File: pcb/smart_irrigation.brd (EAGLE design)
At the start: 100 x 80 mm, 17 parts, among them IC1 7805DT, IC2 7833DT, J1 1X2-3.5MM

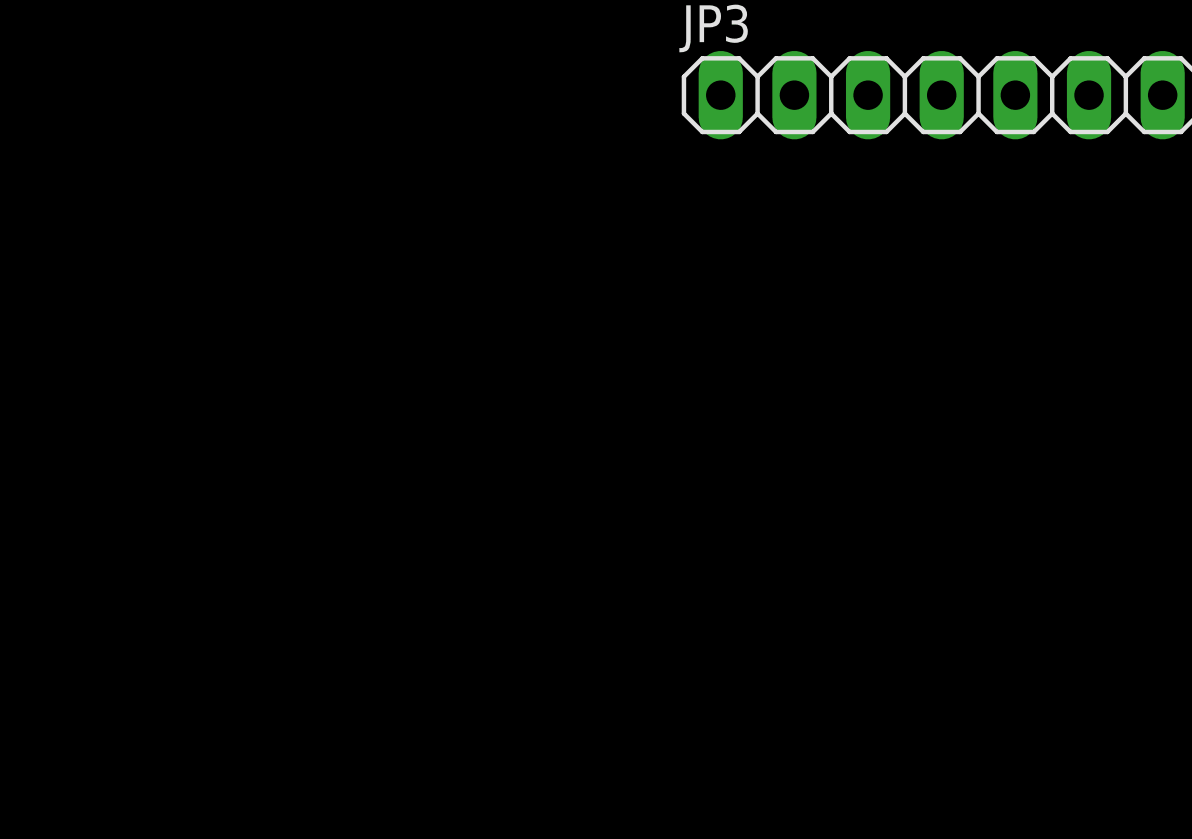
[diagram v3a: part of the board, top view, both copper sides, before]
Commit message: PCB: Add RTC
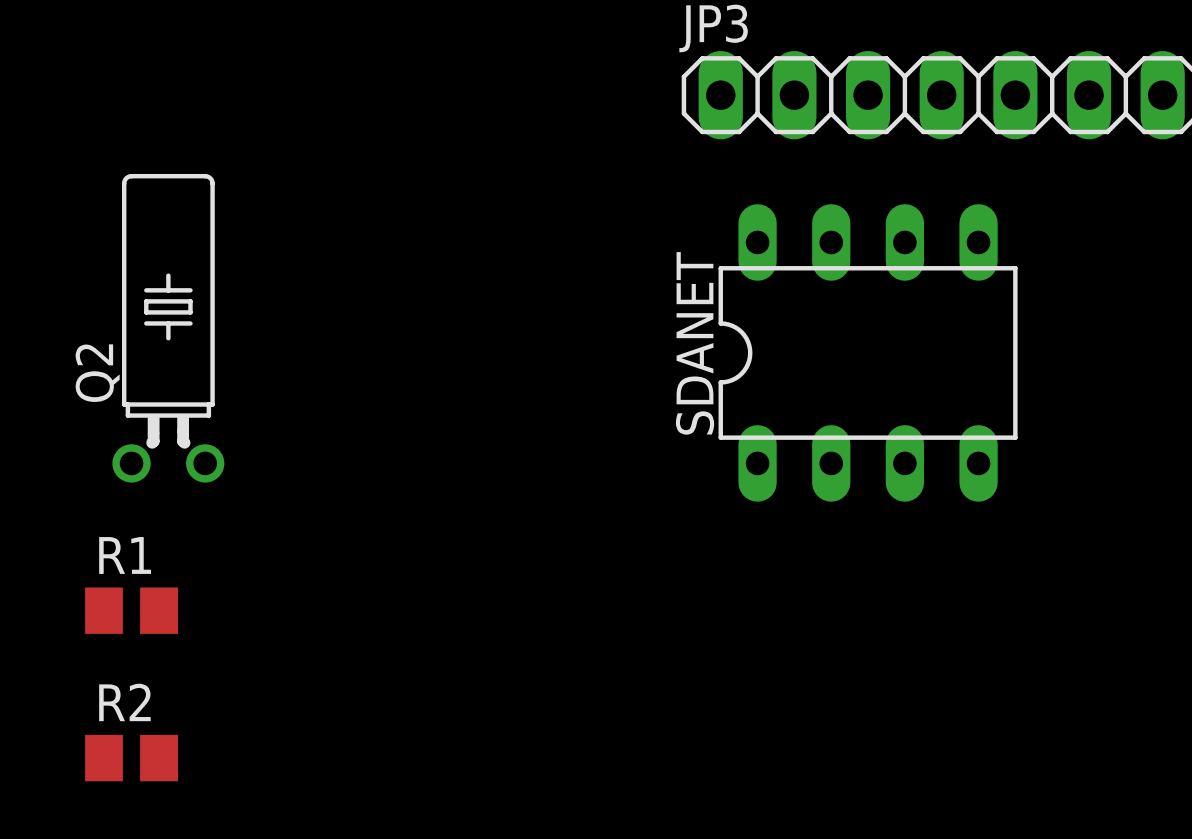
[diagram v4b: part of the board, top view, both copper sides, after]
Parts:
- added Q2: 32.768, crystal:TC38H
- added R1, R2: 2.2k, rcl:M0805
- added SDANET: DS1307, adafruit:DIL08
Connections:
- removed net N$17: JP3.3, U$1.26
- removed net N$28: JP3.14, U$1.13
- removed net N$29: JP3.15, U$1.12
- new net N$15: Q2.2, SDANET.2
- new net N$3: Q2.1, SDANET.1
- new net RTC_OUT: JP3.3, SDANET.7, U$1.26
- new net SCL: JP3.14, R2.1, SDANET.6, U$1.13
- new net SDA: JP3.15, R1.1, SDANET.5, U$1.12
- new net VBAT: SDANET.3
- net +3V3: now also R1.2, R2.2
- net +5V: now also SDANET.8
- net GND: now also SDANET.4
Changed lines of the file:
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@@
 <element name="JP2" library="pinhead" package="1X12" value="" x="-39.37" y="-101.6"/>
 <element name="JP3" library="pinhead" package="1X16" value="" x="-34.29" y="-107.95"/>
+<element name="SDANET" library="adafruit" package="DIL08" value="DS1307" x="-48.26" y="-116.84"/>
+<element name="Q2" library="crystal" package="TC38H" value="32.768" x="-72.39" y="-120.65">
+<attribute name="MPN" value="" x="-72.39" y="-120.65" size="1.778" layer="27" display="off"/>
+<attribute name="OC_NEWARK" value="unknown" x="-72.39" y="-120.65" size="1.778" layer="27" display="off"/>
+<attribute name="OC_FARNELL" value="unknown" x="-72.39" y="-120.65" size="1.778" layer="27" display="off"/>
+<attribute name="MF" value="" x="-72.39" y="-120.65" size="1.778" layer="27" display="off"/>
+</element>
+<element name="R1" library="rcl" package="M0805" value="2.2k" x="-73.66" y="-125.73"/>
+<element name="R2" library="rcl" package="M0805" value="2.2k" x="-73.66" y="-130.81"/>
 </elements>
 <signals>
@@
 <contactref element="U$1" pad="29"/>
 <contactref element="JP2" pad="1"/>
+<contactref element="SDANET" pad="4"/>
+<wire x1="-53.34" y1="-107.95" x2="-44.45" y2="-120.65" width="0" layer="19" extent="1-1"/>
 <wire x1="-53.34" y1="-101.6" x2="-53.34" y2="-107.95" width="0" layer="19" extent="1-1"/>
 <wire x1="-52.07" y1="-95.25" x2="-53.34" y2="-101.6" width="0" layer="19" extent="1-1"/>
@@
 <contactref element="C1" pad="1"/>
 <contactref element="C7" pad="1"/>
+<contactref element="SDANET" pad="8"/>
+<wire x1="-30.16" y1="-63.5" x2="-52.07" y2="-113.03" width="0" layer="19" extent="1-1"/>
 <wire x1="-30.16" y1="-25.4" x2="-30.16" y2="-63.5" width="0" layer="19" extent="1-1"/>
 <wire x1="-4.07" y1="1.55" x2="-30.16" y2="-25.4" width="0" layer="19" extent="1-1"/>
@@
 <contactref element="U$1" pad="J5_3"/>
 <contactref element="U$1" pad="J5_6"/>
+<contactref element="R2" pad="2"/>
+<contactref element="R1" pad="2"/>
+<wire x1="-72.71" y1="-125.73" x2="-72.71" y2="-130.81" width="0" layer="19" extent="1-1"/>
+<wire x1="-46.99" y1="-95.25" x2="-72.71" y2="-125.73" width="0" layer="19" extent="1-1"/>
 <wire x1="-39.37" y1="-95.25" x2="-46.99" y2="-95.25" width="0" layer="19" extent="1-1"/>
 <wire x1="-53.61" y1="-86.13" x2="-46.99" y2="-95.25" width="0" layer="19" extent="1-1"/>
@@
 <wire x1="-33.59" y1="-60.85" x2="-50.8" y2="-107.95" width="0" layer="19" extent="1-1"/>
 </signal>
-<signal name="N$17">
+<signal name="RTC_OUT">
 <contactref element="U$1" pad="26"/>
 <contactref element="JP3" pad="3"/>
+<contactref element="SDANET" pad="7"/>
+<wire x1="-48.26" y1="-107.95" x2="-49.53" y2="-113.03" width="0" layer="19" extent="1-1"/>
 <wire x1="-33.59" y1="-62.12" x2="-48.26" y2="-107.95" width="0" layer="19" extent="1-1"/>
 </signal>
@@
 <wire x1="-33.59" y1="-74.82" x2="-22.86" y2="-107.95" width="0" layer="19" extent="1-1"/>
 </signal>
-<signal name="N$28">
+<signal name="SCL">
 <contactref element="JP3" pad="14"/>
 <contactref element="U$1" pad="13"/>
+<contactref element="SDANET" pad="6"/>
+<contactref element="R2" pad="1"/>
+<wire x1="-46.99" y1="-113.03" x2="-74.61" y2="-130.81" width="0" layer="19" extent="1-1"/>
+<wire x1="-20.32" y1="-107.95" x2="-46.99" y2="-113.03" width="0" layer="19" extent="1-1"/>
 <wire x1="-33.59" y1="-76.09" x2="-20.32" y2="-107.95" width="0" layer="19" extent="1-1"/>
 </signal>
-<signal name="N$29">
+<signal name="SDA">
 <contactref element="U$1" pad="12"/>
 <contactref element="JP3" pad="15"/>
+<contactref element="SDANET" pad="5"/>
+<contactref element="R1" pad="1"/>
+<wire x1="-44.45" y1="-113.03" x2="-74.61" y2="-125.73" width="0" layer="19" extent="1-1"/>
+<wire x1="-17.78" y1="-107.95" x2="-44.45" y2="-113.03" width="0" layer="19" extent="1-1"/>
 <wire x1="-33.59" y1="-77.36" x2="-17.78" y2="-107.95" width="0" layer="19" extent="1-1"/>
 </signal>
+<signal name="VBAT">
+<contactref element="SDANET" pad="3"/>
+</signal>
+<signal name="N$3">
+<contactref element="SDANET" pad="1"/>
+<contactref element="Q2" pad="1"/>
+<wire x1="-52.07" y1="-120.65" x2="-73.66" y2="-120.65" width="0" layer="19" extent="1-1"/>
+</signal>
+<signal name="N$15">
+<contactref element="Q2" pad="2"/>
+<contactref element="SDANET" pad="2"/>
+<wire x1="-49.53" y1="-120.65" x2="-71.12" y2="-120.65" width="0" layer="19" extent="1-1"/>
+</signal>
 </signals>

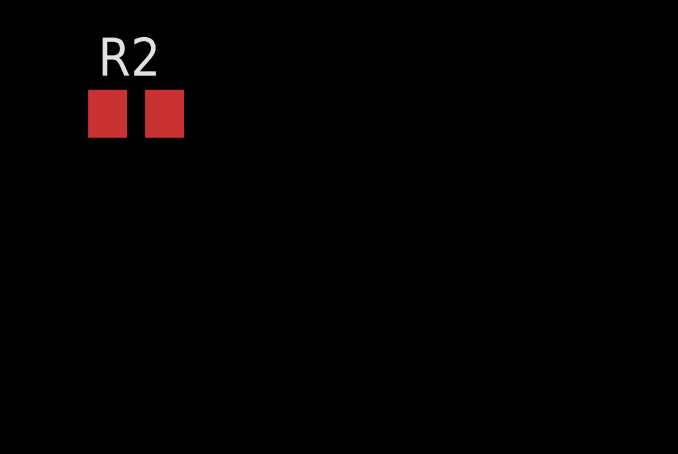
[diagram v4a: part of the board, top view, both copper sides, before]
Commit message: PCB: Add temp sensor
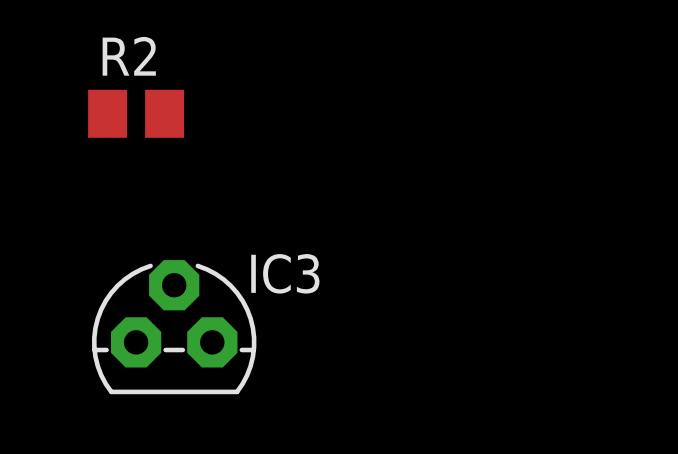
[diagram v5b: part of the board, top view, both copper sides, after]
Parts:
- added IC3: TMP36, smart_irrigation:TO92
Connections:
- removed net N$9: JP2.7, U$1.2
- new net TEMP_OUT: IC3.2, JP2.7, U$1.2
- net +3V3: now also IC3.1
- net GND: now also IC3.3
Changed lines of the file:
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@@
 <element name="R1" library="rcl" package="M0805" value="2.2k" x="-73.66" y="-125.73"/>
 <element name="R2" library="rcl" package="M0805" value="2.2k" x="-73.66" y="-130.81"/>
+<element name="IC3" library="smart_irrigation" package="TO92" value="TMP36" x="-72.39" y="-138.43"/>
 </elements>
 <signals>
@@
 <contactref element="JP2" pad="1"/>
 <contactref element="SDANET" pad="4"/>
+<contactref element="IC3" pad="3"/>
+<wire x1="-44.45" y1="-120.65" x2="-71.12" y2="-138.43" width="0" layer="19" extent="1-1"/>
 <wire x1="-53.34" y1="-107.95" x2="-44.45" y2="-120.65" width="0" layer="19" extent="1-1"/>
 <wire x1="-53.34" y1="-101.6" x2="-53.34" y2="-107.95" width="0" layer="19" extent="1-1"/>
@@
 <contactref element="R2" pad="2"/>
 <contactref element="R1" pad="2"/>
+<contactref element="IC3" pad="1"/>
+<wire x1="-72.71" y1="-130.81" x2="-73.66" y2="-138.43" width="0" layer="19" extent="1-1"/>
 <wire x1="-72.71" y1="-125.73" x2="-72.71" y2="-130.81" width="0" layer="19" extent="1-1"/>
 <wire x1="-46.99" y1="-95.25" x2="-72.71" y2="-125.73" width="0" layer="19" extent="1-1"/>
@@
 <wire x1="-53.64" y1="-65.97" x2="-40.64" y2="-101.6" width="0" layer="19" extent="1-1"/>
 </signal>
-<signal name="N$9">
+<signal name="TEMP_OUT">
 <contactref element="JP2" pad="7"/>
 <contactref element="U$1" pad="2"/>
+<contactref element="IC3" pad="2"/>
+<wire x1="-38.1" y1="-101.6" x2="-72.39" y2="-136.525" width="0" layer="19" extent="1-1"/>
 <wire x1="-53.64" y1="-67.24" x2="-38.1" y2="-101.6" width="0" layer="19" extent="1-1"/>
 </signal>

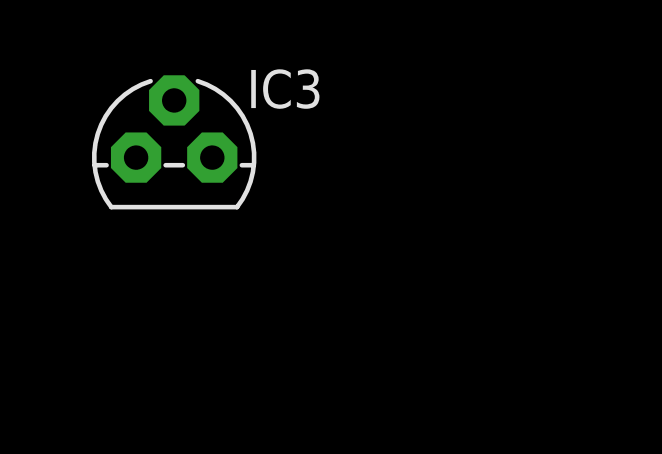
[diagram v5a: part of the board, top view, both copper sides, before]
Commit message: PCB: Add soil moisture sensor
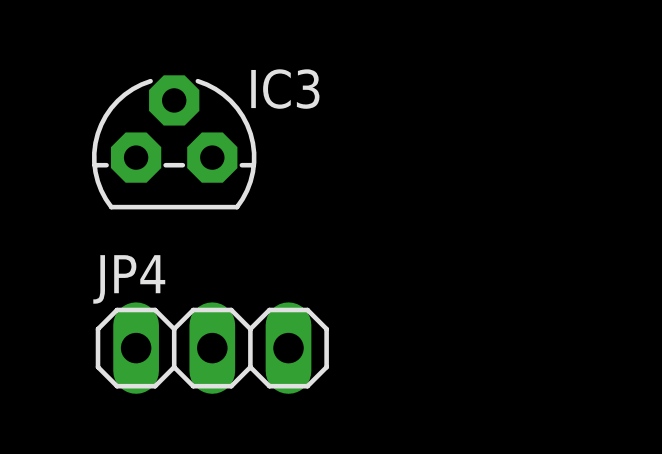
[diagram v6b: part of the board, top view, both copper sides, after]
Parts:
- added JP4: (no value), pinhead:1X03
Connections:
- removed net N$10: JP2.8, U$1.4
- new net SMS_OUT: JP2.8, JP4.3, U$1.4
- net +3V3: now also JP4.1
- net GND: now also JP4.2
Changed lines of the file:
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@@
 <element name="R2" library="rcl" package="M0805" value="2.2k" x="-73.66" y="-130.81"/>
 <element name="IC3" library="smart_irrigation" package="TO92" value="TMP36" x="-72.39" y="-138.43"/>
+<element name="JP4" library="pinhead" package="1X03" value="" x="-71.12" y="-144.78"/>
 </elements>
 <signals>
@@
 <contactref element="SDANET" pad="4"/>
 <contactref element="IC3" pad="3"/>
+<contactref element="JP4" pad="2"/>
+<wire x1="-71.12" y1="-138.43" x2="-71.12" y2="-144.78" width="0" layer="19" extent="1-1"/>
 <wire x1="-44.45" y1="-120.65" x2="-71.12" y2="-138.43" width="0" layer="19" extent="1-1"/>
 <wire x1="-53.34" y1="-107.95" x2="-44.45" y2="-120.65" width="0" layer="19" extent="1-1"/>
@@
 <contactref element="R1" pad="2"/>
 <contactref element="IC3" pad="1"/>
+<contactref element="JP4" pad="1"/>
+<wire x1="-73.66" y1="-138.43" x2="-73.66" y2="-144.78" width="0" layer="19" extent="1-1"/>
 <wire x1="-72.71" y1="-130.81" x2="-73.66" y2="-138.43" width="0" layer="19" extent="1-1"/>
 <wire x1="-72.71" y1="-125.73" x2="-72.71" y2="-130.81" width="0" layer="19" extent="1-1"/>
@@
 <wire x1="-53.64" y1="-67.24" x2="-38.1" y2="-101.6" width="0" layer="19" extent="1-1"/>
 </signal>
-<signal name="N$10">
+<signal name="SMS_OUT">
 <contactref element="U$1" pad="4"/>
 <contactref element="JP2" pad="8"/>
+<contactref element="JP4" pad="3"/>
+<wire x1="-35.56" y1="-101.6" x2="-68.58" y2="-144.78" width="0" layer="19" extent="1-1"/>
 <wire x1="-53.64" y1="-68.51" x2="-35.56" y2="-101.6" width="0" layer="19" extent="1-1"/>
 </signal>

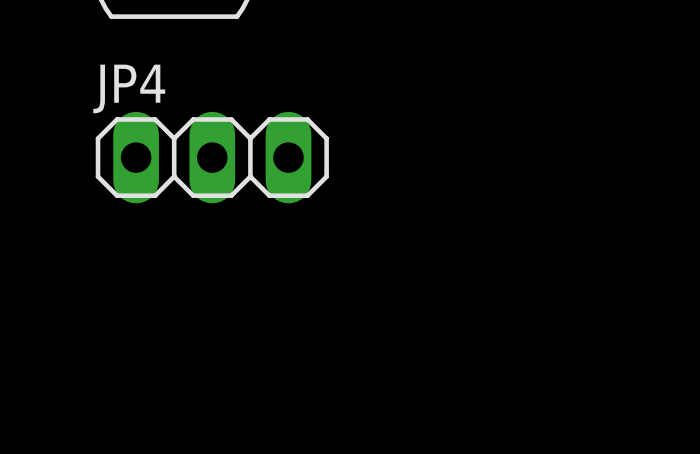
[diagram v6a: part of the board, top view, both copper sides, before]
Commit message: PCB: Add raindrop sensor
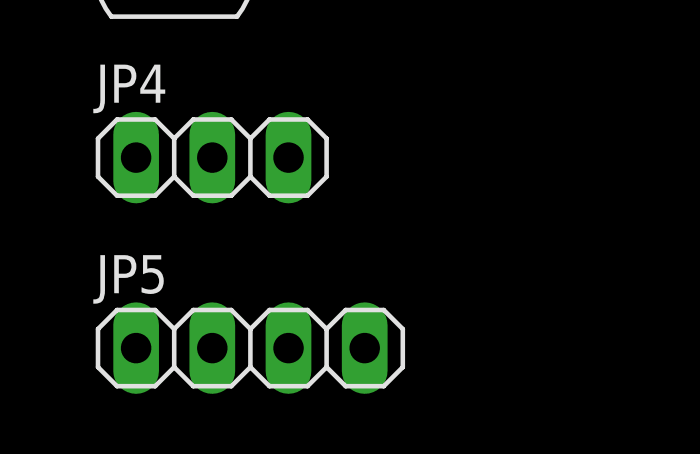
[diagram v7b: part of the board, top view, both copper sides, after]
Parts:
- added JP5: (no value), smart_irrigation:1X04
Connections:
- net N$1 renamed NAUTORUN
- net SMS_OUT renamed SOIL_OUT
- removed net N$11: JP2.9, U$1.5
- new net RAIN_OUT: JP2.9, JP5.4, U$1.5
- net +3V3: now also JP5.1
- net GND: now also JP5.2
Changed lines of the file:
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@@
 <element name="IC3" library="smart_irrigation" package="TO92" value="TMP36" x="-72.39" y="-138.43"/>
 <element name="JP4" library="pinhead" package="1X03" value="" x="-71.12" y="-144.78"/>
+<element name="JP5" library="smart_irrigation" package="1X04" value="" x="-69.85" y="-151.13"/>
 </elements>
 <signals>
@@
 <contactref element="JP3" pad="16"/>
 <contactref element="U$1" pad="11"/>
-<contactref element="U$1" pad="28"/>
-<contactref element="JP3" pad="1"/>
-<contactref element="U$1" pad="29"/>
-<contactref element="JP2" pad="1"/>
 <contactref element="SDANET" pad="4"/>
 <contactref element="IC3" pad="3"/>
 <contactref element="JP4" pad="2"/>
+<contactref element="JP5" pad="2"/>
+<contactref element="U$1" pad="29"/>
+<contactref element="JP2" pad="1"/>
+<contactref element="U$1" pad="28"/>
+<contactref element="JP3" pad="1"/>
+<wire x1="-71.12" y1="-144.78" x2="-71.12" y2="-151.13" width="0" layer="19" extent="1-1"/>
 <wire x1="-71.12" y1="-138.43" x2="-71.12" y2="-144.78" width="0" layer="19" extent="1-1"/>
 <wire x1="-44.45" y1="-120.65" x2="-71.12" y2="-138.43" width="0" layer="19" extent="1-1"/>
@@
 <contactref element="IC3" pad="1"/>
 <contactref element="JP4" pad="1"/>
+<contactref element="JP5" pad="1"/>
+<wire x1="-73.66" y1="-144.78" x2="-73.66" y2="-151.13" width="0" layer="19" extent="1-1"/>
 <wire x1="-73.66" y1="-138.43" x2="-73.66" y2="-144.78" width="0" layer="19" extent="1-1"/>
 <wire x1="-72.71" y1="-130.81" x2="-73.66" y2="-138.43" width="0" layer="19" extent="1-1"/>
@@
 <wire x1="-23.12" y1="-77.19" x2="-22.54" y2="-81.28" width="0" layer="19" extent="1-1"/>
 </signal>
-<signal name="N$1">
+<signal name="NAUTORUN">
 <contactref element="U$1" pad="J5_2"/>
 <contactref element="JP1" pad="2"/>
@@
 <wire x1="-53.64" y1="-67.24" x2="-38.1" y2="-101.6" width="0" layer="19" extent="1-1"/>
 </signal>
-<signal name="SMS_OUT">
+<signal name="SOIL_OUT">
 <contactref element="U$1" pad="4"/>
 <contactref element="JP2" pad="8"/>
@@
 <wire x1="-53.64" y1="-68.51" x2="-35.56" y2="-101.6" width="0" layer="19" extent="1-1"/>
 </signal>
-<signal name="N$11">
+<signal name="RAIN_OUT">
 <contactref element="JP2" pad="9"/>
 <contactref element="U$1" pad="5"/>
+<contactref element="JP5" pad="4"/>
+<wire x1="-33.02" y1="-101.6" x2="-66.04" y2="-151.13" width="0" layer="19" extent="1-1"/>
 <wire x1="-53.64" y1="-69.78" x2="-33.02" y2="-101.6" width="0" layer="19" extent="1-1"/>
 </signal>
